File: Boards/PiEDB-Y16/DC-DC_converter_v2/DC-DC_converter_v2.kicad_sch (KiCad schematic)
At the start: 20 parts

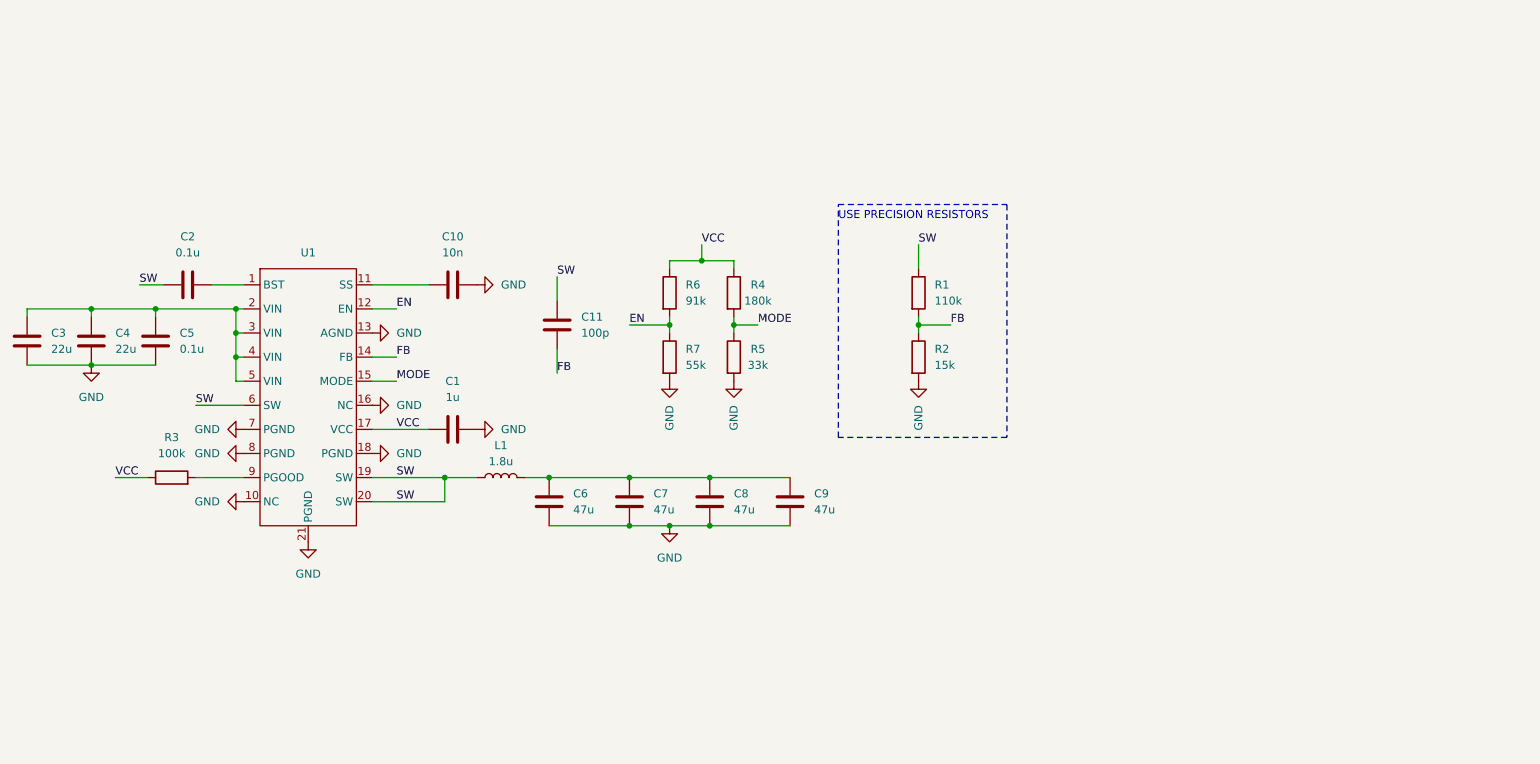
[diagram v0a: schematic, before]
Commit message: roughly finished layout for new dc-dc converter
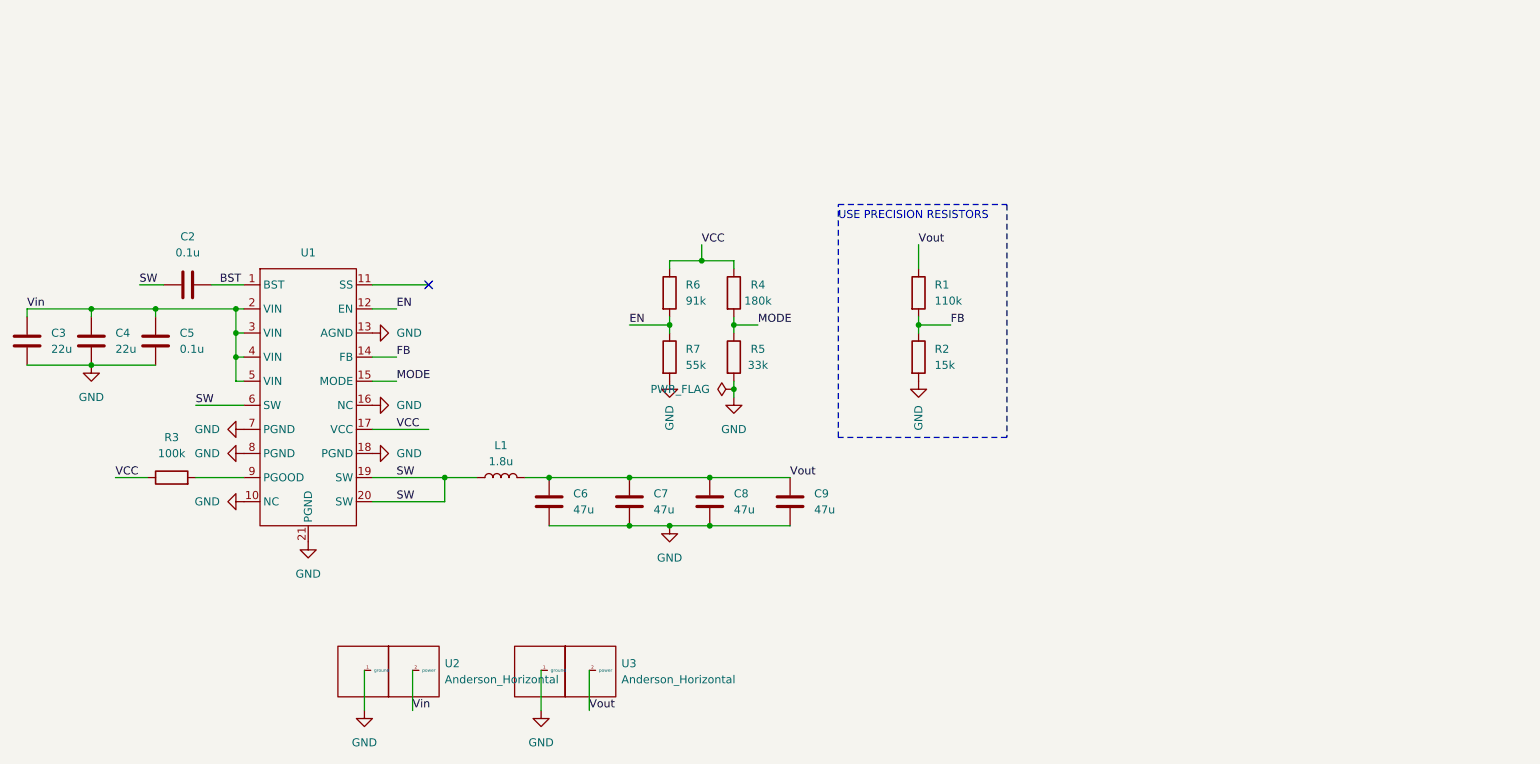
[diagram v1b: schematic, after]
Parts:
- removed C1: 1u, Capacitor_SMD:C_0805_2012Metric, symbol Device:C
- removed C10: 10n, Capacitor_SMD:C_0805_2012Metric, symbol Device:C
- removed C11: 100p, Capacitor_SMD:C_0603_1608Metric, symbol Device:C
- added U2, U3: Anderson_Horizontal, PiE_Footprints:anderson_horizontal, symbol PiE_Symbols:Anderson_Horizontal
- L1: footprint PiE_Footprints:IND_IHLP-5050CE_VIS -> PiE_Footprints:125CDMCCDS-1R8MC
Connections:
- net GND: now also U2.1 (ground), U3.1 (ground)
- net SW: no longer R1.1
- net Vout: now reaches C6.2, C7.2, C8.2, C9.2, L1.2
- net Vout: now also R1.1, U3.2 (power)
- net Vin: now reaches C3.2, C4.2, C5.2, U1.2 (VIN), U1.3 (VIN), U1.4 (VIN), U1.5 (VIN)
- net Vin: now also U2.2 (power)
- net BST: now reaches C2.2, U1.1 (BST)
- no-connect marks 0 -> 1

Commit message: updated BOM
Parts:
- R4: value 180k -> 200k
- R6: value 91k -> 100k
- R7: value 55k -> 51k
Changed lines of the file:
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@@
       (effects (font (size 1.27 1.27)) (justify left))
     )
-    (property "Value" "55k" (at 152.4 69.85 0)
+    (property "Value" "51k" (at 152.4 69.85 0)
       (effects (font (size 1.27 1.27)) (justify left))
     )
@@
       (effects (font (size 1.27 1.27)))
     )
-    (property "Value" "180k" (at 163.83 59.69 0)
+    (property "Value" "200k" (at 163.83 59.69 0)
       (effects (font (size 1.27 1.27)))
     )
@@
       (effects (font (size 1.27 1.27)) (justify left))
     )
-    (property "Value" "91k" (at 152.4 59.69 0)
-      (effects (font (size 1.27 1.27)) (justify left))
-    )
+    (property "Value" "100k" (at 152.4 59.69 0)
+      (effects (font (size 1.27 1.27)) (justify left))
+    )

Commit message: made contingency board
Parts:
- added C1: 1uF, Capacitor_SMD:C_0603_1608Metric_Pad1.08x0.95mm_HandSolder, symbol Device:C
- added J1: 2 Pins, Connector_PinHeader_2.54mm:PinHeader_1x02_P2.54mm_Vertical, symbol Connector:Conn_01x02_Pin
- R7: value 51k -> 15k
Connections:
- net EN: now also J1.2 (Pin_2); no longer R6.2, R7.1
- net GND: now also C1.2
- net VCC: no longer R6.1
- net Vin: now also R6.1
- net at U1.11 (SS): now also C1.1
- new net: J1.1 (Pin_1), R6.2, R7.1
- no-connect marks 1 -> 0
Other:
- moved on the sheet: R1, R2, R4, R5, R6, R7
